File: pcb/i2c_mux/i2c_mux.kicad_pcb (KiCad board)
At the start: 2 copper layers, 99.1 x 96.5 mm, 33 parts, among them J1 RJ45, J2 RJ45, J3 RJ45, J4 RJ45, J5 RJ45, J6 RJ45, J7 RJ45, J8 RJ45, J9 RJ45, U1 Adafruit_TCA6548A

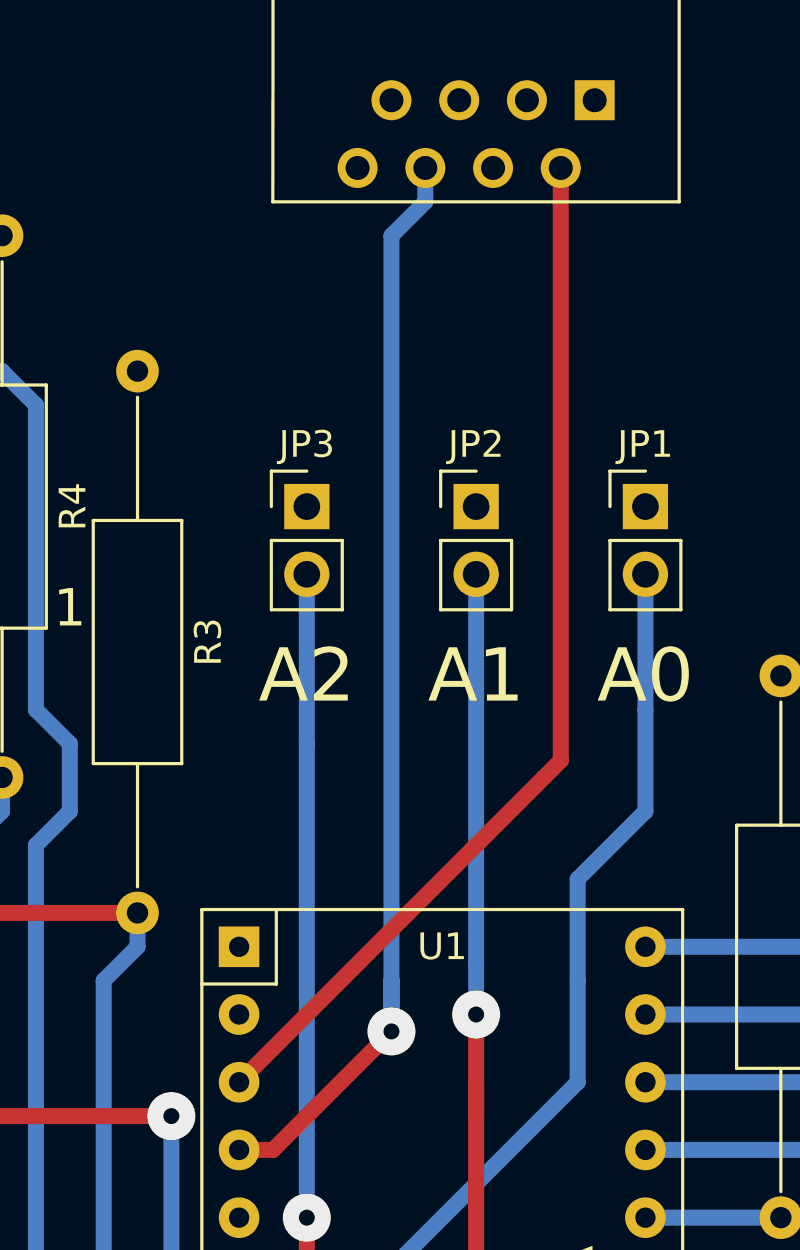
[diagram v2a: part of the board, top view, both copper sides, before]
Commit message: Fix SDA/SCL mix-up and pull RST up
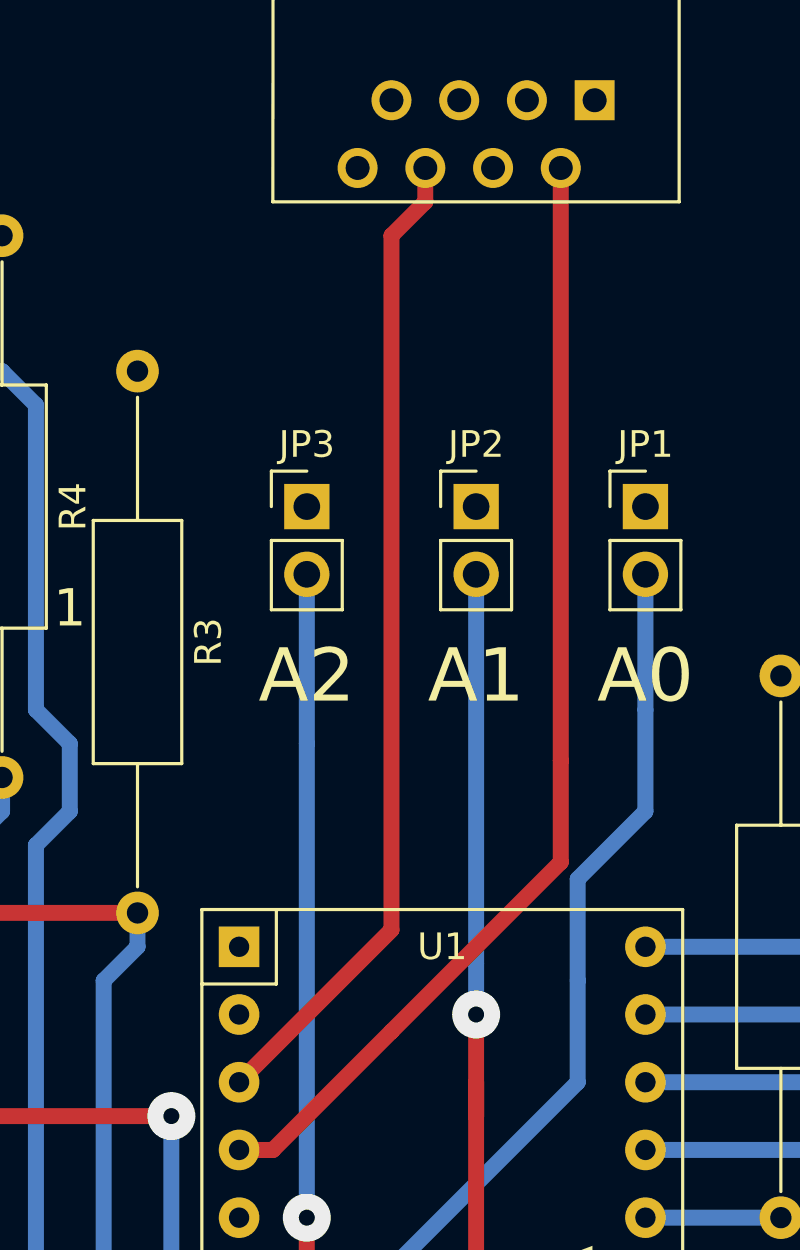
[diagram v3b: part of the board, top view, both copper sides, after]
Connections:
- U1 pad 3: Net-(J9-Pad2) -> Net-(J9-Pad6)
- U1 pad 4: Net-(J9-Pad6) -> Net-(J9-Pad2)
- U1 pad 5: Net-(U1-Pad5) -> VCC
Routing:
- net Net-(J9-Pad6): track 42.4 -> 37.2 mm, vias 1 -> 0
- net Net-(J9-Pad2): track 39.3 -> 42.6 mm
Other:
- board text added: "v1.10 20171213"
- board text removed: "v1.02 20171114"
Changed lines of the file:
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@@
 (kicad_pcb (version 4) (host pcbnew 4.0.7-e2-6376~58~ubuntu17.04.1)
   (general
-    (links 74)
+    (links 75)
     (no_connects 0)
     (area 85.292857 49.035 200.89 152.560001)
     (thickness 1.6)
     (drawings 28)
-    (tracks 167)
+    (tracks 165)
     (zones 0)
     (modules 33)
-    (nets 61)
+    (nets 60)
   )
   (page A4)
@@
   (net 58 "Net-(JP2-Pad2)")
   (net 59 "Net-(JP3-Pad2)")
-  (net 60 "Net-(U1-Pad5)")
   (net_class Default "This is the default net class."
     (clearance 0.6)
@@
     (add_net "Net-(JP2-Pad2)")
     (add_net "Net-(JP3-Pad2)")
-    (add_net "Net-(U1-Pad5)")
     (add_net VCC)
   )
@@
       (net 1 GND))
     (pad 3 thru_hole circle (at 0 5.08) (size 1.524 1.524) (drill 0.762) (layers *.Cu *.Mask)
+      (net 54 "Net-(J9-Pad6)"))
+    (pad 4 thru_hole circle (at 0 7.62) (size 1.524 1.524) (drill 0.762) (layers *.Cu *.Mask)
       (net 51 "Net-(J9-Pad2)"))
-    (pad 4 thru_hole circle (at 0 7.62) (size 1.524 1.524) (drill 0.762) (layers *.Cu *.Mask)
-      (net 54 "Net-(J9-Pad6)"))
     (pad 5 thru_hole circle (at 0 10.16) (size 1.524 1.524) (drill 0.762) (layers *.Cu *.Mask)
-      (net 60 "Net-(U1-Pad5)"))
+      (net 3 VCC))
     (pad 6 thru_hole circle (at 0 12.7) (size 1.524 1.524) (drill 0.762) (layers *.Cu *.Mask)
       (net 57 "Net-(JP1-Pad2)"))
@@
     (effects (font (size 1.4 1.4) (thickness 0.3)))
   )
-  (gr_text "v1.02 20171114" (at 110.49 140.97) (layer B.SilkS)
+  (gr_text "v1.10 20171213" (at 110.49 140.97) (layer B.SilkS)
     (effects (font (size 1.4 1.4) (thickness 0.3)) (justify mirror))
   )
@@
   (segment (start 163.83 91.44) (end 163.83 78.74) (width 0.6) (layer B.Cu) (net 48))
   (segment (start 156.21 99.06) (end 163.83 91.44) (width 0.6) (layer B.Cu) (net 48))
+  (segment (start 142.875 89.535) (end 142.875 93.345) (width 0.6) (layer F.Cu) (net 51))
+  (segment (start 142.875 93.345) (end 136.525 99.695) (width 0.6) (layer F.Cu) (net 51))
   (segment (start 142.875 67.31) (end 142.875 89.535) (width 0.6) (layer F.Cu) (net 51))
-  (segment (start 142.875 89.535) (end 142.24 90.17) (width 0.6) (layer F.Cu) (net 51))
-  (segment (start 142.24 90.17) (end 130.81 101.6) (width 0.6) (layer F.Cu) (net 51))
-  (segment (start 130.81 104.14) (end 132.08 104.14) (width 0.6) (layer F.Cu) (net 54))
-  (via (at 136.525 99.695) (size 1.8) (drill 0.6) (layers F.Cu B.Cu) (net 54))
-  (segment (start 132.08 104.14) (end 136.525 99.695) (width 0.6) (layer F.Cu) (net 54))
-  (segment (start 136.525 99.695) (end 136.525 97.79) (width 0.6) (layer B.Cu) (net 54))
-  (segment (start 136.525 69.85) (end 136.525 97.79) (width 0.6) (layer B.Cu) (net 54))
-  (segment (start 136.525 97.79) (end 136.525 99.695) (width 0.6) (layer B.Cu) (net 54))
-  (segment (start 137.795 67.31) (end 137.795 68.58) (width 0.6) (layer B.Cu) (net 54))
-  (segment (start 137.795 68.58) (end 136.525 69.85) (width 0.6) (layer B.Cu) (net 54))
+  (segment (start 130.81 104.14) (end 132.08 104.14) (width 0.6) (layer F.Cu) (net 51))
+  (segment (start 132.08 104.14) (end 136.525 99.695) (width 0.6) (layer F.Cu) (net 51))
+  (segment (start 137.795 67.31) (end 137.795 68.58) (width 0.6) (layer F.Cu) (net 54))
+  (segment (start 136.525 69.85) (end 136.525 95.885) (width 0.6) (layer F.Cu) (net 54))
+  (segment (start 137.795 68.58) (end 136.525 69.85) (width 0.6) (layer F.Cu) (net 54))
+  (segment (start 136.525 95.885) (end 130.81 101.6) (width 0.6) (layer F.Cu) (net 54))
   (segment (start 146.05 87.63) (end 146.05 91.44) (width 0.6) (layer B.Cu) (net 57))
   (segment (start 146.05 91.44) (end 143.51 93.98) (width 0.6) (layer B.Cu) (net 57))

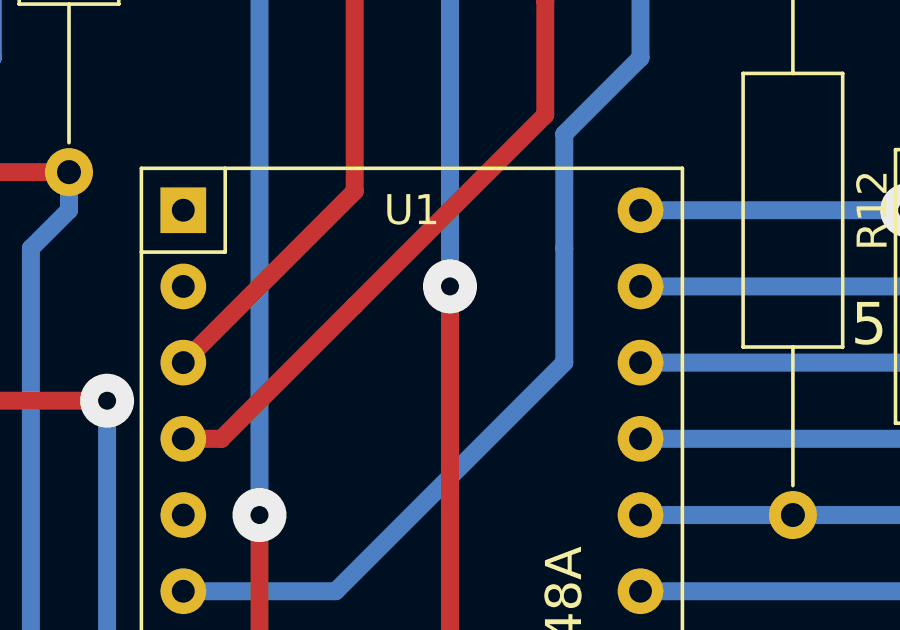
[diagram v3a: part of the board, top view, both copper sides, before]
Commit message: Pull address selectors up instead of down and move a via
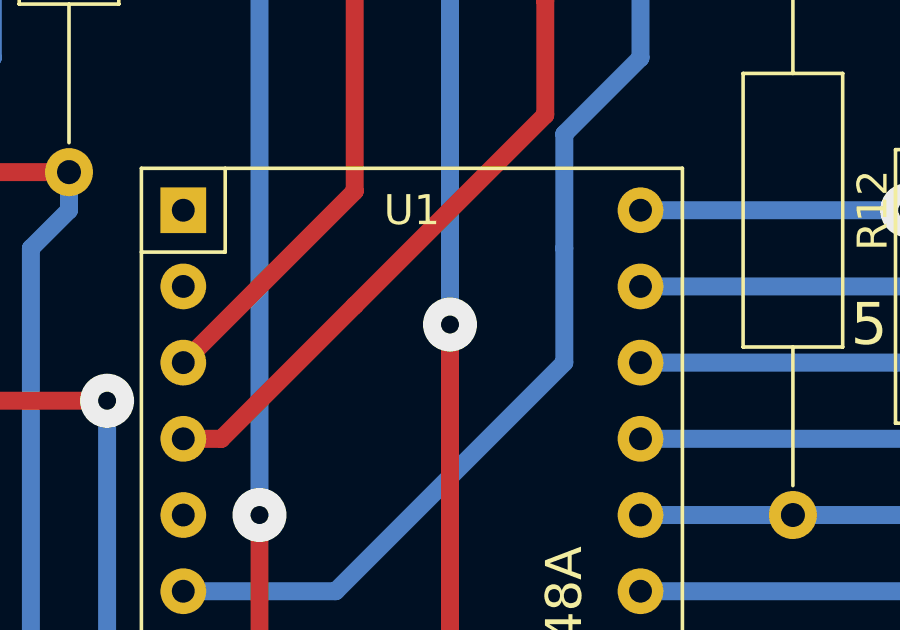
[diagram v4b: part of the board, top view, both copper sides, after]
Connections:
- JP1 pad 1: GND -> VCC
- JP2 pad 1: GND -> VCC
- JP3 pad 1: GND -> VCC
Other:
- board text added: "v1.11 20171213"
- board text removed: "v1.10 20171213"
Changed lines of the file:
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@@
   (general
     (links 75)
-    (no_connects 0)
+    (no_connects 1)
     (area 85.292857 49.035 200.89 152.560001)
     (thickness 1.6)
@@
     )
     (pad 1 thru_hole rect (at 0 0) (size 1.7 1.7) (drill 1) (layers *.Cu *.Mask)
-      (net 1 GND))
+      (net 3 VCC))
     (pad 2 thru_hole oval (at 0 2.54) (size 1.7 1.7) (drill 1) (layers *.Cu *.Mask)
       (net 57 "Net-(JP1-Pad2)"))
@@
     )
     (pad 1 thru_hole rect (at 0 0) (size 1.7 1.7) (drill 1) (layers *.Cu *.Mask)
-      (net 1 GND))
+      (net 3 VCC))
     (pad 2 thru_hole oval (at 0 2.54) (size 1.7 1.7) (drill 1) (layers *.Cu *.Mask)
       (net 58 "Net-(JP2-Pad2)"))
@@
     )
     (pad 1 thru_hole rect (at 0 0) (size 1.7 1.7) (drill 1) (layers *.Cu *.Mask)
-      (net 1 GND))
+      (net 3 VCC))
     (pad 2 thru_hole oval (at 0 2.54) (size 1.7 1.7) (drill 1) (layers *.Cu *.Mask)
       (net 59 "Net-(JP3-Pad2)"))
@@
     (effects (font (size 1.4 1.4) (thickness 0.3)))
   )
-  (gr_text "v1.10 20171213" (at 110.49 140.97) (layer B.SilkS)
+  (gr_text "v1.11 20171213" (at 110.49 140.97) (layer B.SilkS)
     (effects (font (size 1.4 1.4) (thickness 0.3)) (justify mirror))
   )
@@
   (segment (start 135.89 109.22) (end 143.51 101.6) (width 0.6) (layer B.Cu) (net 57))
   (segment (start 146.05 82.55) (end 146.05 87.63) (width 0.6) (layer B.Cu) (net 57))
-  (segment (start 139.7 102.87) (end 139.7 99.06) (width 0.6) (layer F.Cu) (net 58))
-  (segment (start 139.7 99.06) (end 139.7 97.155) (width 0.6) (layer B.Cu) (net 58))
-  (via (at 139.7 99.06) (size 1.8) (drill 0.6) (layers F.Cu B.Cu) (net 58))
+  (segment (start 139.7 102.87) (end 139.7 100.33) (width 0.6) (layer F.Cu) (net 58))
+  (segment (start 139.7 100.33) (end 139.7 97.155) (width 0.6) (layer B.Cu) (net 58))
+  (via (at 139.7 100.33) (size 1.8) (drill 0.6) (layers F.Cu B.Cu) (net 58))
   (segment (start 138.43 111.76) (end 139.7 111.76) (width 0.6) (layer B.Cu) (net 58))
   (segment (start 139.7 111.76) (end 139.7 102.87) (width 0.6) (layer F.Cu) (net 58))
